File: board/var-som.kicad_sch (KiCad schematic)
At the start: 5 parts, among them U1 VAR-SOM

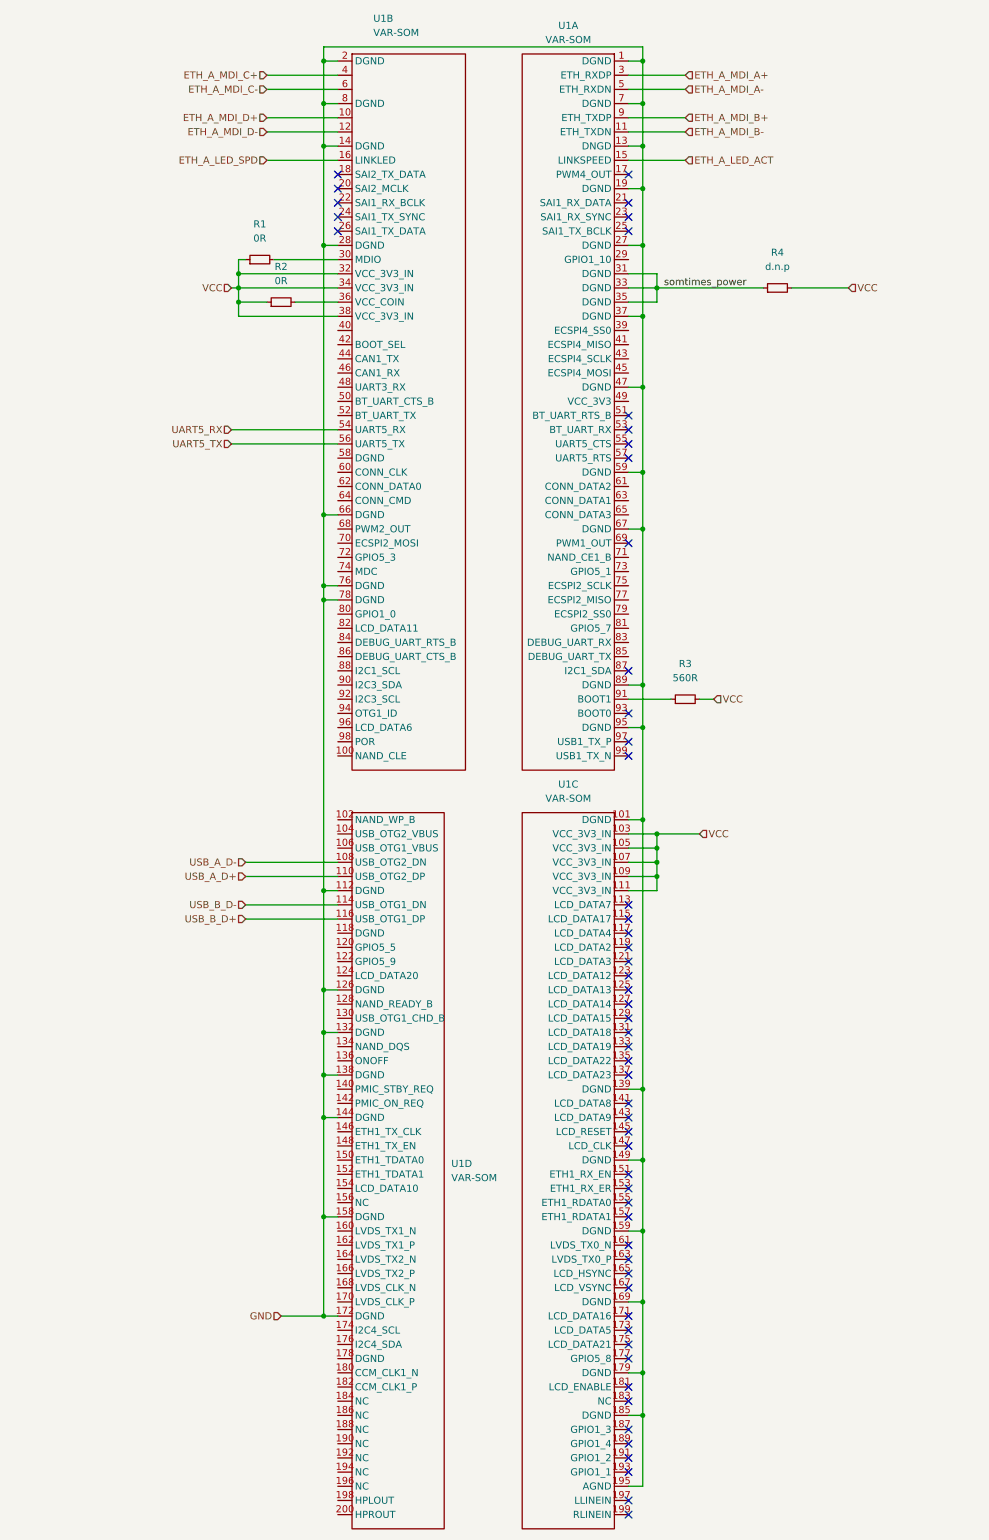
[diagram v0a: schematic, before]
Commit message: added RGMII interface
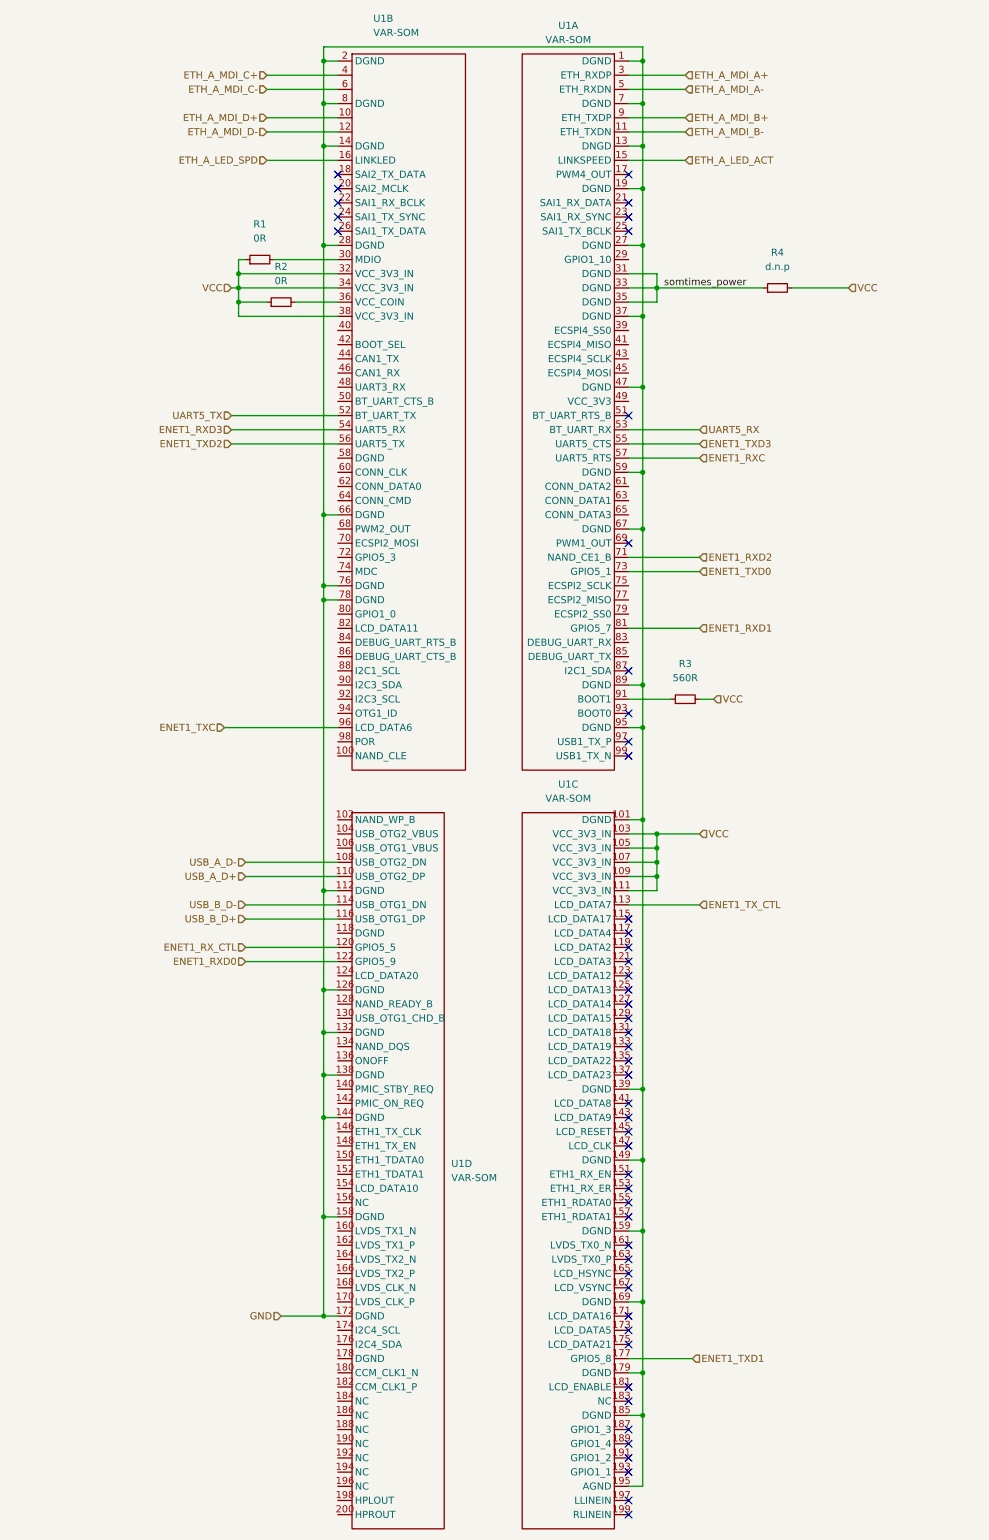
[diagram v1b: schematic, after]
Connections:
- net UART5_RX: now also U1.53 (BT_UART_RX); no longer U1.54 (UART5_RX)
- net UART5_TX: now also U1.52 (BT_UART_TX); no longer U1.56 (UART5_TX)
- net ENET1_TXD3: now reaches U1.55 (UART5_CTS)
- net ENET1_RXC: now reaches U1.57 (UART5_RTS)
- net ENET1_RXD2: now reaches U1.71 (NAND_CE1_B)
- net ENET1_TXD0: now reaches U1.73 (GPIO5_1)
- net ENET1_RXD1: now reaches U1.81 (GPIO5_7)
- net ENET1_TX_CTL: now reaches U1.113 (LCD_DATA7)
- net ENET1_TXD1: now reaches U1.177 (GPIO5_8)
- net ENET1_TXC: now reaches U1.96 (LCD_DATA6)
- net ENET1_RX_CTL: now reaches U1.120 (GPIO5_5)
- net ENET1_RXD0: now reaches U1.122 (GPIO5_9)
- new net ENET1_RXD3: U1.54 (UART5_RX)
- new net ENET1_TXD2: U1.56 (UART5_TX)
- no-connect marks 55 -> 50
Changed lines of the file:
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@@
   (no_connect (at 167.64 142.24))
   (no_connect (at 167.64 137.16))
-  (no_connect (at 167.64 91.44))
-  (no_connect (at 167.64 88.9))
-  (no_connect (at 167.64 86.36))
   (no_connect (at 167.64 237.49))
   (no_connect (at 167.64 234.95))
@@
   (no_connect (at 167.64 176.53))
   (no_connect (at 167.64 173.99))
-  (no_connect (at 167.64 171.45))
   (no_connect (at 167.64 260.35))
   (no_connect (at 167.64 257.81))
-  (no_connect (at 167.64 252.73))
   (no_connect (at 167.64 250.19))
   (no_connect (at 167.64 280.67))
@@
     (stroke (width 0) (type default) (color 0 0 0 0))
   )
+  (wire (pts (xy 95.25 139.7) (xy 115.57 139.7))
+    (stroke (width 0) (type default) (color 0 0 0 0))
+  )
   (wire (pts (xy 170.18 229.87) (xy 170.18 242.57))
     (stroke (width 0) (type default) (color 0 0 0 0))
@@
     (stroke (width 0) (type default) (color 0 0 0 0))
   )
+  (wire (pts (xy 167.64 121.92) (xy 180.34 121.92))
+    (stroke (width 0) (type default) (color 0 0 0 0))
+  )
   (wire (pts (xy 97.79 58.42) (xy 115.57 58.42))
     (stroke (width 0) (type default) (color 0 0 0 0))
@@
     (stroke (width 0) (type default) (color 0 0 0 0))
   )
+  (wire (pts (xy 167.64 171.45) (xy 180.34 171.45))
+    (stroke (width 0) (type default) (color 0 0 0 0))
+  )
   (wire (pts (xy 167.64 78.74) (xy 170.18 78.74))
     (stroke (width 0) (type default) (color 0 0 0 0))
@@
     (stroke (width 0) (type default) (color 0 0 0 0))
   )
+  (wire (pts (xy 167.64 109.22) (xy 180.34 109.22))
+    (stroke (width 0) (type default) (color 0 0 0 0))
+  )
   (wire (pts (xy 102.87 33.02) (xy 115.57 33.02))
     (stroke (width 0) (type default) (color 0 0 0 0))
   )
+  (wire (pts (xy 167.64 111.76) (xy 180.34 111.76))
+    (stroke (width 0) (type default) (color 0 0 0 0))
+  )
   (wire (pts (xy 170.18 156.21) (xy 170.18 204.47))
     (stroke (width 0) (type default) (color 0 0 0 0))
@@
     (stroke (width 0) (type default) (color 0 0 0 0))
   )
+  (wire (pts (xy 167.64 252.73) (xy 179.07 252.73))
+    (stroke (width 0) (type default) (color 0 0 0 0))
+  )
   (wire (pts (xy 167.64 25.4) (xy 177.8 25.4))
     (stroke (width 0) (type default) (color 0 0 0 0))
@@
     (stroke (width 0) (type default) (color 0 0 0 0))
   )
+  (wire (pts (xy 99.06 181.61) (xy 115.57 181.61))
+    (stroke (width 0) (type default) (color 0 0 0 0))
+  )
   (wire (pts (xy 167.64 60.96) (xy 172.72 60.96))
     (stroke (width 0) (type default) (color 0 0 0 0))
@@
     (stroke (width 0) (type default) (color 0 0 0 0))
   )
+  (wire (pts (xy 167.64 86.36) (xy 180.34 86.36))
+    (stroke (width 0) (type default) (color 0 0 0 0))
+  )
   (wire (pts (xy 113.03 53.34) (xy 113.03 35.56))
     (stroke (width 0) (type default) (color 0 0 0 0))
@@
     (stroke (width 0) (type default) (color 0 0 0 0))
   )
+  (wire (pts (xy 96.52 83.82) (xy 115.57 83.82))
+    (stroke (width 0) (type default) (color 0 0 0 0))
+  )
   (wire (pts (xy 167.64 217.17) (xy 170.18 217.17))
     (stroke (width 0) (type default) (color 0 0 0 0))
@@
     (stroke (width 0) (type default) (color 0 0 0 0))
   )
+  (wire (pts (xy 99.06 179.07) (xy 115.57 179.07))
+    (stroke (width 0) (type default) (color 0 0 0 0))
+  )
   (wire (pts (xy 172.72 163.83) (xy 172.72 161.29))
     (stroke (width 0) (type default) (color 0 0 0 0))
@@
   )
   (wire (pts (xy 97.79 58.42) (xy 97.79 55.88))
+    (stroke (width 0) (type default) (color 0 0 0 0))
+  )
+  (wire (pts (xy 167.64 88.9) (xy 180.34 88.9))
+    (stroke (width 0) (type default) (color 0 0 0 0))
+  )
+  (wire (pts (xy 167.64 91.44) (xy 180.34 91.44))
     (stroke (width 0) (type default) (color 0 0 0 0))
   )
@@
     (effects (font (size 1.27 1.27)) (justify left bottom))
   )
+  (hierarchical_label "ENET1_TXD3" (shape input) (at 180.34 88.9 0)
+    (effects (font (size 1.27 1.27)) (justify left))
+  )
+  (hierarchical_label "ENET1_TXD1" (shape input) (at 179.07 252.73 0)
+    (effects (font (size 1.27 1.27)) (justify left))
+  )
   (hierarchical_label "ETH_A_LED_ACT" (shape input) (at 177.8 38.1 0)
     (effects (font (size 1.27 1.27)) (justify left))
   )
-  (hierarchical_label "UART5_TX" (shape input) (at 96.52 88.9 180)
+  (hierarchical_label "UART5_TX" (shape input) (at 96.52 83.82 180)
+    (effects (font (size 1.27 1.27)) (justify right))
+  )
+  (hierarchical_label "ENET1_RXD0" (shape input) (at 99.06 181.61 180)
     (effects (font (size 1.27 1.27)) (justify right))
   )
@@
     (effects (font (size 1.27 1.27)) (justify right))
   )
+  (hierarchical_label "ENET1_RXD1" (shape input) (at 180.34 121.92 0)
+    (effects (font (size 1.27 1.27)) (justify left))
+  )
   (hierarchical_label "USB_B_D-" (shape input) (at 99.06 171.45 180)
     (effects (font (size 1.27 1.27)) (justify right))
@@
     (effects (font (size 1.27 1.27)) (justify left))
   )
+  (hierarchical_label "ENET1_TXC" (shape input) (at 95.25 139.7 180)
+    (effects (font (size 1.27 1.27)) (justify right))
+  )
   (hierarchical_label "GND" (shape input) (at 105.41 245.11 180)
     (effects (font (size 1.27 1.27)) (justify right))
@@
     (effects (font (size 1.27 1.27)) (justify right))
   )
+  (hierarchical_label "ENET1_TX_CTL" (shape input) (at 180.34 171.45 0)
+    (effects (font (size 1.27 1.27)) (justify left))
+  )
   (hierarchical_label "USB_A_D+" (shape input) (at 99.06 166.37 180)
     (effects (font (size 1.27 1.27)) (justify right))
   )
-  (hierarchical_label "UART5_RX" (shape input) (at 96.52 86.36 180)
-    (effects (font (size 1.27 1.27)) (justify right))
+  (hierarchical_label "UART5_RX" (shape input) (at 180.34 86.36 0)
+    (effects (font (size 1.27 1.27)) (justify left))
   )
   (hierarchical_label "ETH_A_MDI_B-" (shape input) (at 177.8 33.02 0)
     (effects (font (size 1.27 1.27)) (justify left))
   )
+  (hierarchical_label "ENET1_TXD0" (shape input) (at 180.34 111.76 0)
+    (effects (font (size 1.27 1.27)) (justify left))
+  )
+  (hierarchical_label "ENET1_RXC" (shape input) (at 180.34 91.44 0)
+    (effects (font (size 1.27 1.27)) (justify left))
+  )
+  (hierarchical_label "ENET1_RXD3" (shape input) (at 96.52 86.36 180)
+    (effects (font (size 1.27 1.27)) (justify right))
+  )
   (hierarchical_label "USB_A_D-" (shape input) (at 99.06 163.83 180)
     (effects (font (size 1.27 1.27)) (justify right))
@@
     (effects (font (size 1.27 1.27)) (justify left))
   )
+  (hierarchical_label "ENET1_RXD2" (shape input) (at 180.34 109.22 0)
+    (effects (font (size 1.27 1.27)) (justify left))
+  )
   (hierarchical_label "ETH_A_MDI_B+" (shape input) (at 177.8 30.48 0)
     (effects (font (size 1.27 1.27)) (justify left))
@@
     (effects (font (size 1.27 1.27)) (justify right))
   )
+  (hierarchical_label "ENET1_RX_CTL" (shape input) (at 99.06 179.07 180)
+    (effects (font (size 1.27 1.27)) (justify right))
+  )
   (hierarchical_label "USB_B_D+" (shape input) (at 99.06 173.99 180)
     (effects (font (size 1.27 1.27)) (justify right))
@@
     (effects (font (size 1.27 1.27)) (justify right))
   )
+  (hierarchical_label "ENET1_TXD2" (shape input) (at 96.52 88.9 180)
+    (effects (font (size 1.27 1.27)) (justify right))
+  )

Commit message: added uSD card
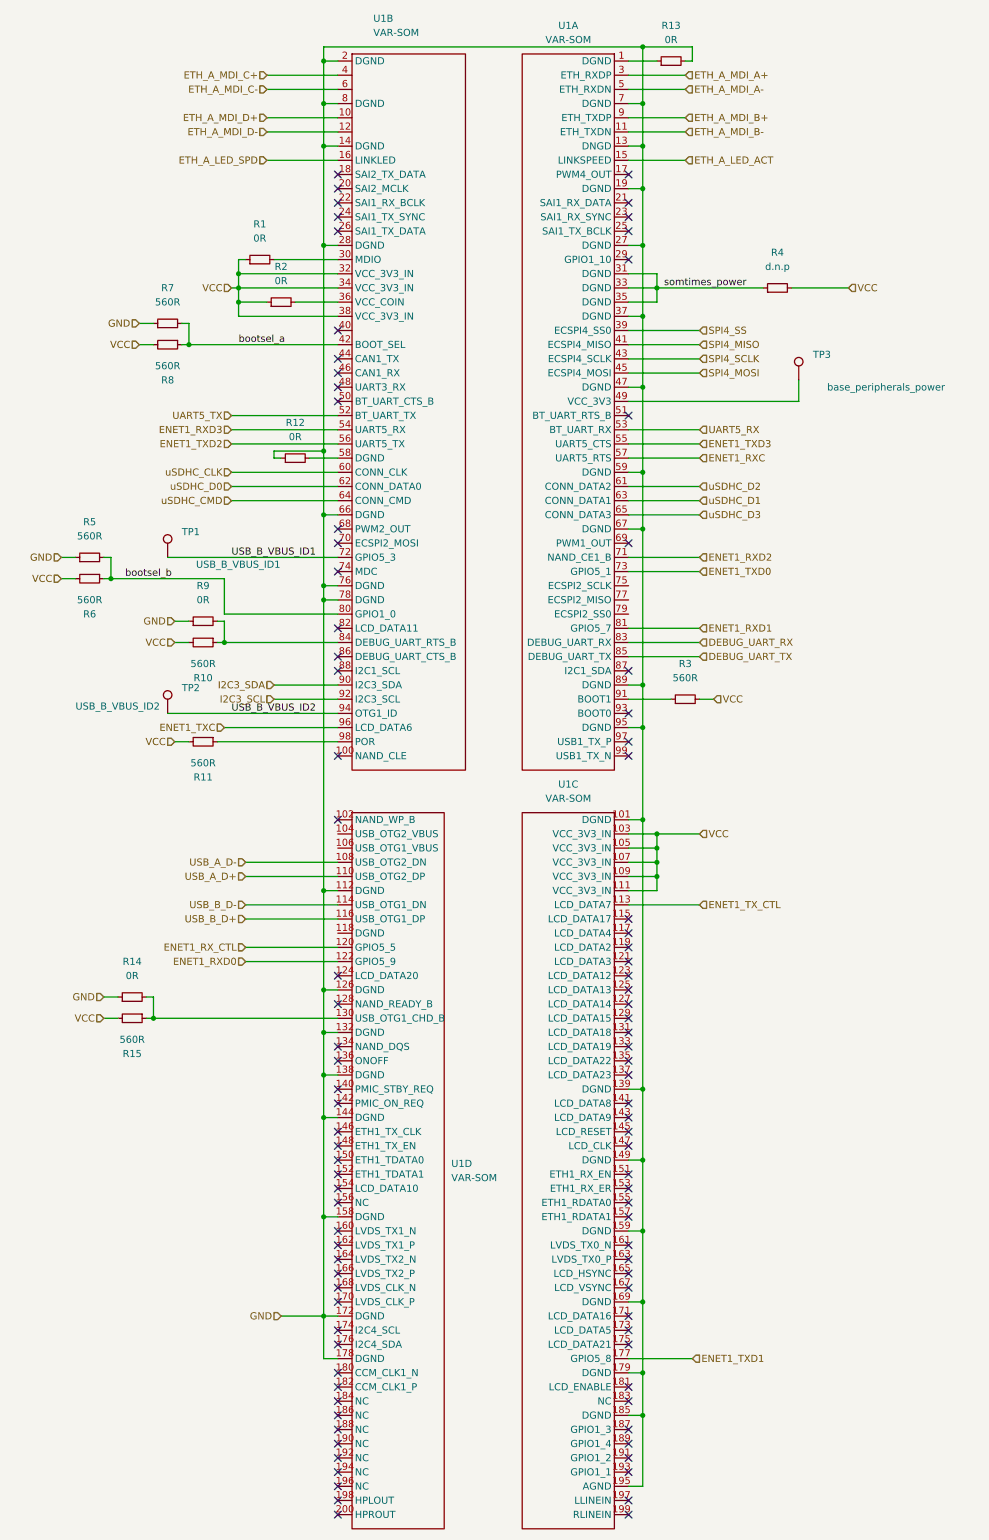
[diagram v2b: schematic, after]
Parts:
- added R10, R11, R15, R5, R6, R7, R8: 560R, Resistor_SMD:R_0603_1608Metric, symbol Device:R_Small
- added R12, R13, R14, R9: 0R, Resistor_SMD:R_0603_1608Metric, symbol Device:R_Small
- added TP1: USB_B_VBUS_ID1, TestPoint:TestPoint_Pad_1.0x1.0mm, symbol Connector:TestPoint
- added TP2: USB_B_VBUS_ID2, TestPoint:TestPoint_Pad_1.0x1.0mm, symbol Connector:TestPoint
- added TP3: base_peripherals_power, TestPoint:TestPoint_Pad_1.0x1.0mm, symbol Connector:TestPoint
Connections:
- net GND: now also U1.178 (DGND), R12.1, R13.2, R14.1, R5.1, R7.1, R9.1; no longer U1.1 (DGND)
- net VCC: now also R10.2, R11.2, R15.2, R6.2, R8.2
- net SPI4_SS: now reaches U1.39 (ECSPI4_SS0)
- net SPI4_MISO: now reaches U1.41 (ECSPI4_MISO)
- net SPI4_SCLK: now reaches U1.43 (ECSPI4_SCLK)
- net SPI4_MOSI: now reaches U1.45 (ECSPI4_MOSI)
- net at U1.49 (VCC_3V3): now also TP3.1
- net uSDHC_D2: now reaches U1.61 (CONN_DATA2)
- net uSDHC_D1: now reaches U1.63 (CONN_DATA1)
- net uSDHC_D3: now reaches U1.65 (CONN_DATA3)
- net DEBUG_UART_RX: now reaches U1.83 (DEBUG_UART_RX)
- net DEBUG_UART_TX: now reaches U1.85 (DEBUG_UART_TX)
- net bootsel_a: now reaches U1.42 (BOOT_SEL)
- net bootsel_a: now also R7.2, R8.1
- net at U1.58 (DGND): now also R12.2
- net uSDHC_CLK: now reaches U1.60 (CONN_CLK)
- net uSDHC_D0: now reaches U1.62 (CONN_DATA0)
- net uSDHC_CMD: now reaches U1.64 (CONN_CMD)
- net USB_B_VBUS_ID1: now reaches U1.72 (GPIO5_3)
- net USB_B_VBUS_ID1: now also TP1.1
- net bootsel_b: now reaches U1.80 (GPIO1_0)
- net bootsel_b: now also R5.2, R6.1
- net at U1.84 (DEBUG_UART_RTS_B): now also R10.1, R9.2
- net I2C3_SDA: now reaches U1.90 (I2C3_SDA)
- net I2C3_SCL: now reaches U1.92 (I2C3_SCL)
- net USB_B_VBUS_ID2: now reaches U1.94 (OTG1_ID)
- net USB_B_VBUS_ID2: now also TP2.1
- net at U1.98 (POR): now also R11.1
- net at U1.130 (USB_OTG1_CHD_B): now also R14.2, R15.1
- new net: R13.1, U1.1 (DGND)
- no-connect marks 50 -> 95

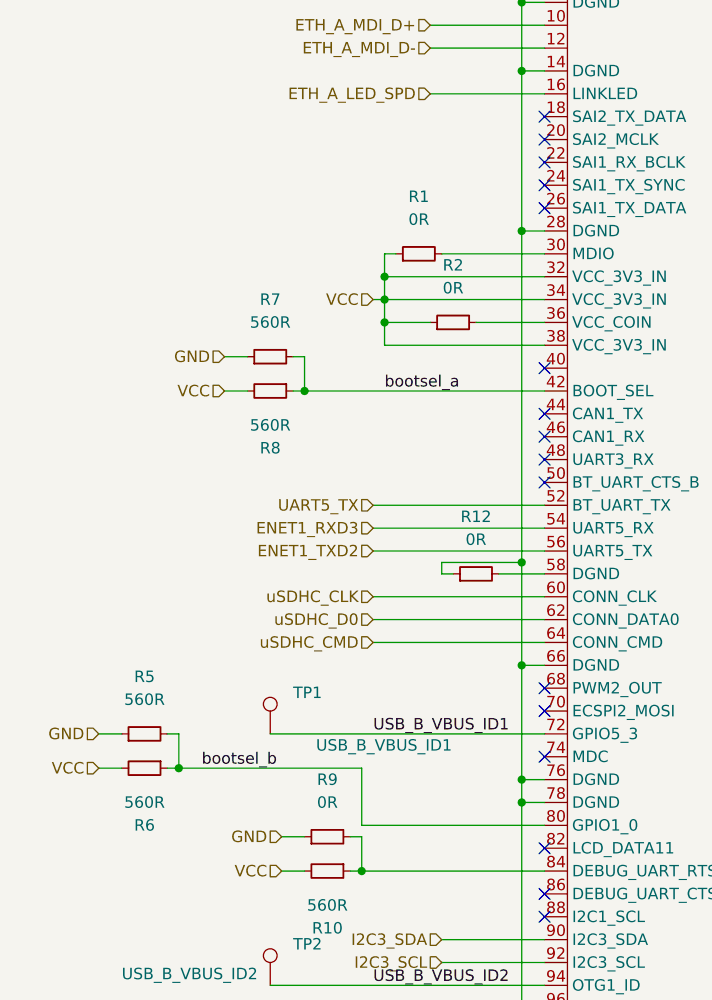
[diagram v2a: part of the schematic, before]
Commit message: added 1.8v power option for RGMII IO
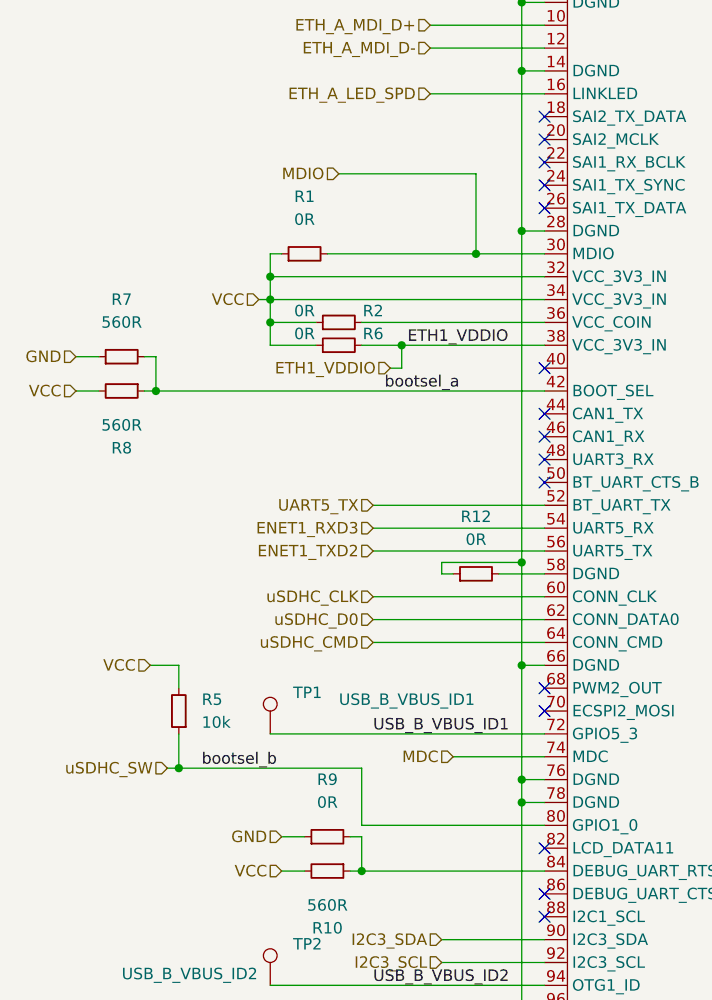
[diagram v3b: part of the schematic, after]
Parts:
- R5: value 560R -> 10k
- R6: value 560R -> 0R
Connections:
- net GND: no longer R5.1
- net VCC: now also R5.2, R6.1; no longer R6.2, U1.38 (VCC_3V3_IN)
- net MDIO: now reaches R1.2, U1.30 (MDIO)
- net MDC: now reaches U1.74 (MDC)
- removed net bootsel_b: R5.2, R6.1, U1.80 (GPIO1_0)
- new net ETH1_VDDIO: R6.2, U1.38 (VCC_3V3_IN)
- new net uSDHC_SW: R5.1, U1.80 (GPIO1_0)
- no-connect marks 95 -> 94
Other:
- moved on the sheet: R1, R2, R7, R8
